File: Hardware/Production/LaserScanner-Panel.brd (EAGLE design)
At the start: 66 x 77.5 mm, 90 parts, among them J1 USB, J2 !KILL!, J3 KEYSWITCH, J5 ESTOP, J8 Power Input, Q1 MBT3904DW1T1, Q4 2.5A/30V/105mΩ, U1 ESP-WROOM-32, U2 3.3V, U3 CH340C

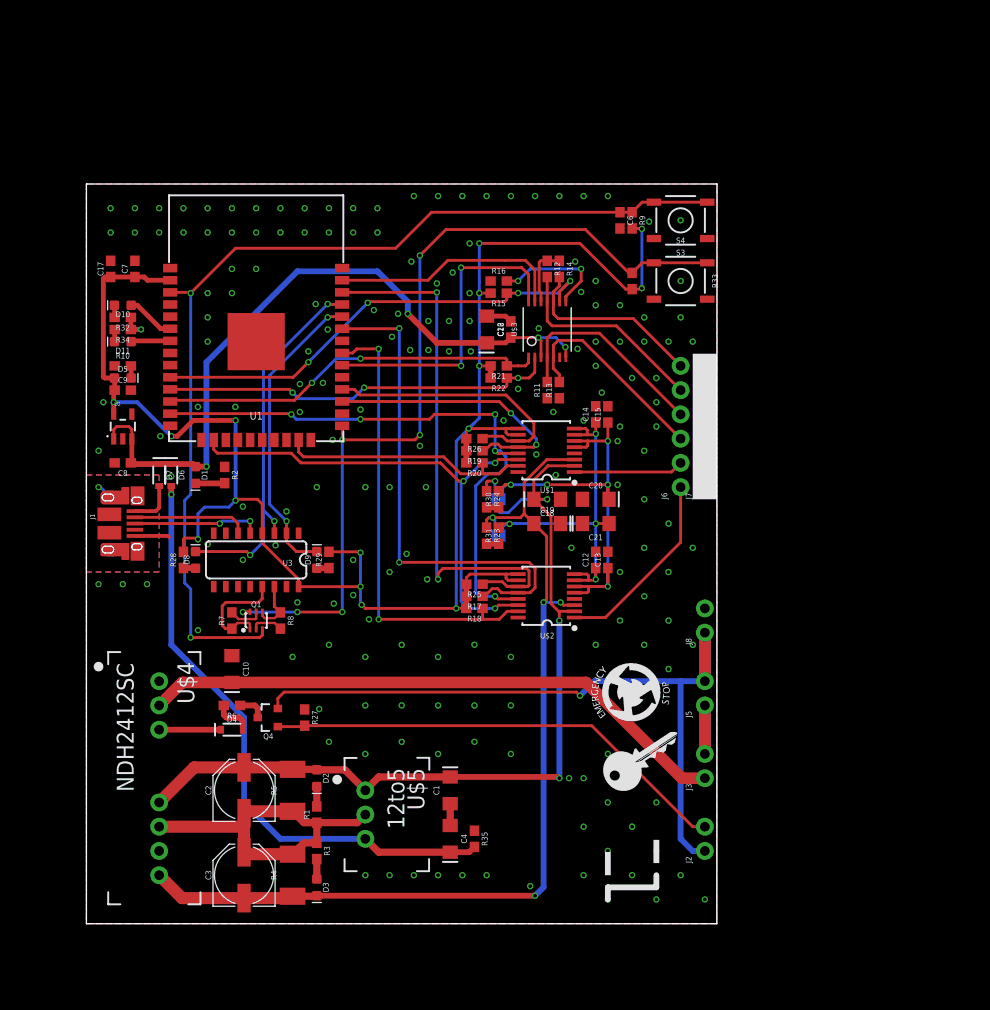
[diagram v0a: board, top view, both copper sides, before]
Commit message: Added silk, optimized ground planes, and cammed
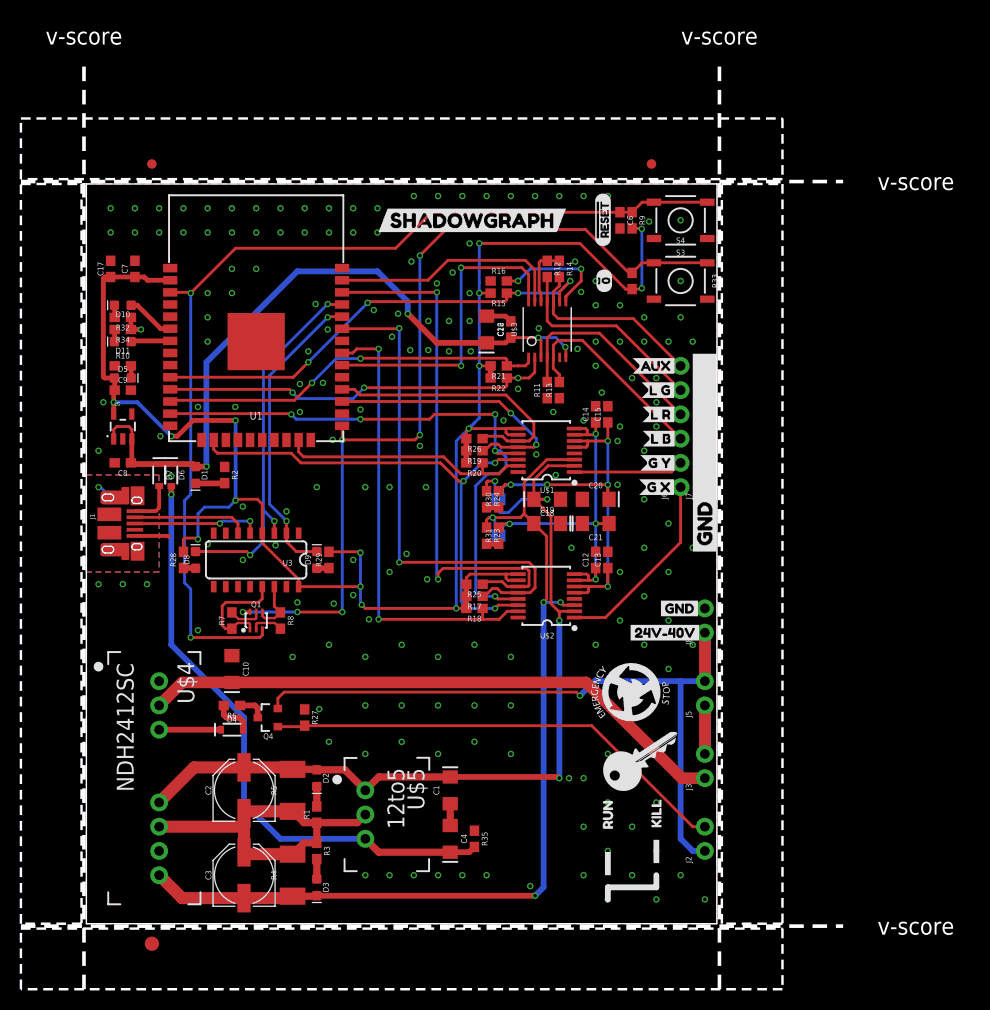
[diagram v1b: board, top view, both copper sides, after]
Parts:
- removed FRAME1: FRAME-LEDGER, SparkFun-Aesthetics:CREATIVE_COMMONS
- added E$1, E$2: (no value), SparkFun-Aesthetics:FIDUCIAL-1X2
- added E$3: (no value), SparkFun-Retired:FIDUCIAL-1.5X3
- added U$10: (no value), buzzard_labels:GND1
- added U$11: (no value), buzzard_labels:KILL11
- added U$12: (no value), buzzard_labels:RUN10
- added U$13: (no value), buzzard_labels:#RESET14
- added U$14: (no value), buzzard_labels:#013
- added U$15: (no value), buzzard_labels:AUX4
- added U$16: (no value), buzzard_labels:G_X14
- added U$17: (no value), buzzard_labels:G_Y13
- added U$18: (no value), buzzard_labels:L_B12
- added U$19: (no value), buzzard_labels:LPF_BYPASS12
- added U$20: (no value), buzzard_labels:L_R14
- added U$21: (no value), buzzard_labels:L_G10
- added U$22: (no value), buzzard_labels:SHADOWGRAPH15
- added U$8: (no value), buzzard_labels:24V#40V3
- added U$9: (no value), buzzard_labels:GND0
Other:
- board size 66 x 77.5 mm -> 86.1 x 97.5 mm
- board text added: "v-score"
